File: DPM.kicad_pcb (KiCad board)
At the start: 2 copper layers, 95.9 x 90.2 mm, 27 parts, among them J1 Conn_02x12_Odd_Even, J2 Conn_02x05_Odd_Even, U1 74LS251, U25 74LS85, U28 74LS85, U3 ADG333A, U31 74LS85, U4 MCP23017_SP, U5 ADG333A, U6 ADG333A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

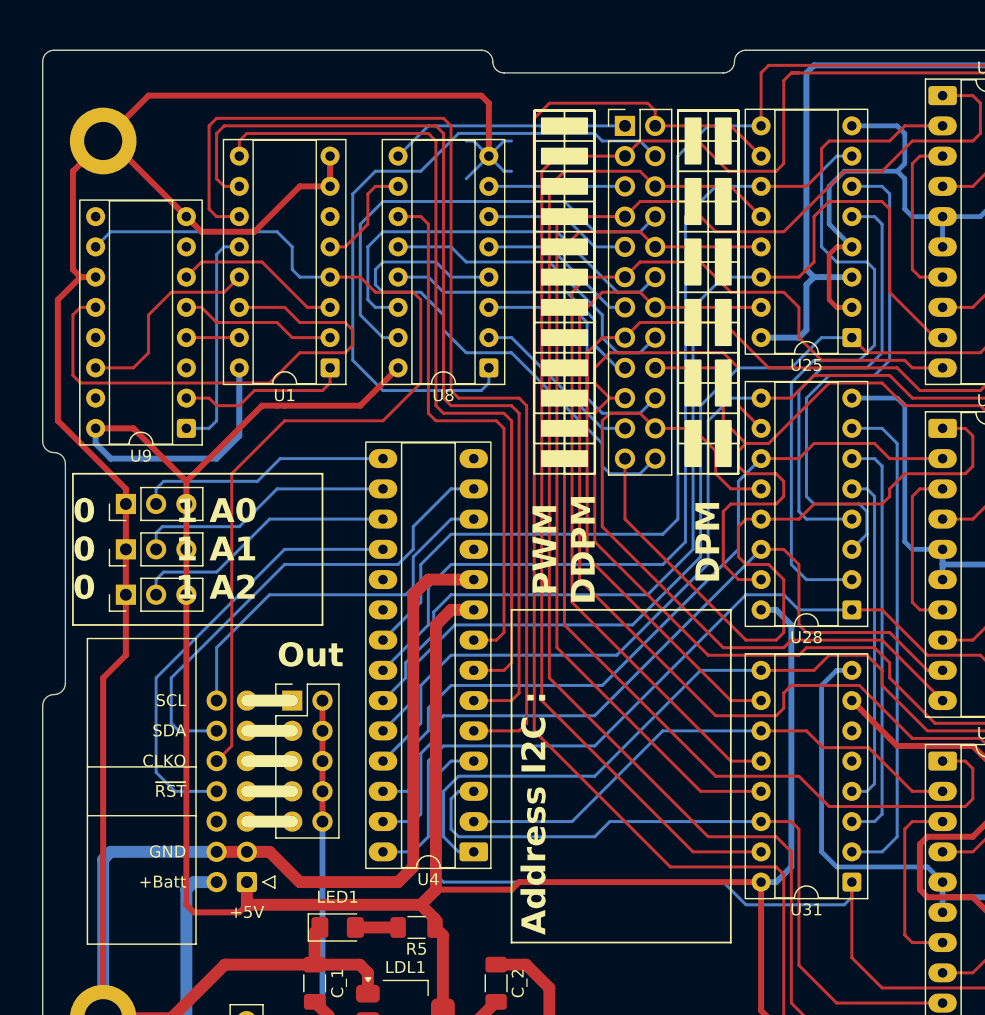
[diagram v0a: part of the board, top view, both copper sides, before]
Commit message: Nouvelle liste de prescaler : 1 2 8 16 64 256 1024 4096
git-svn-id: file:///D%5C00%20-%20Dev%20&%20Calculs%5CRepoTortoiseSVN_PCB%5CD-DPM/trunk@21 f29d8339-a183-0348-962e-9e4594cf8312
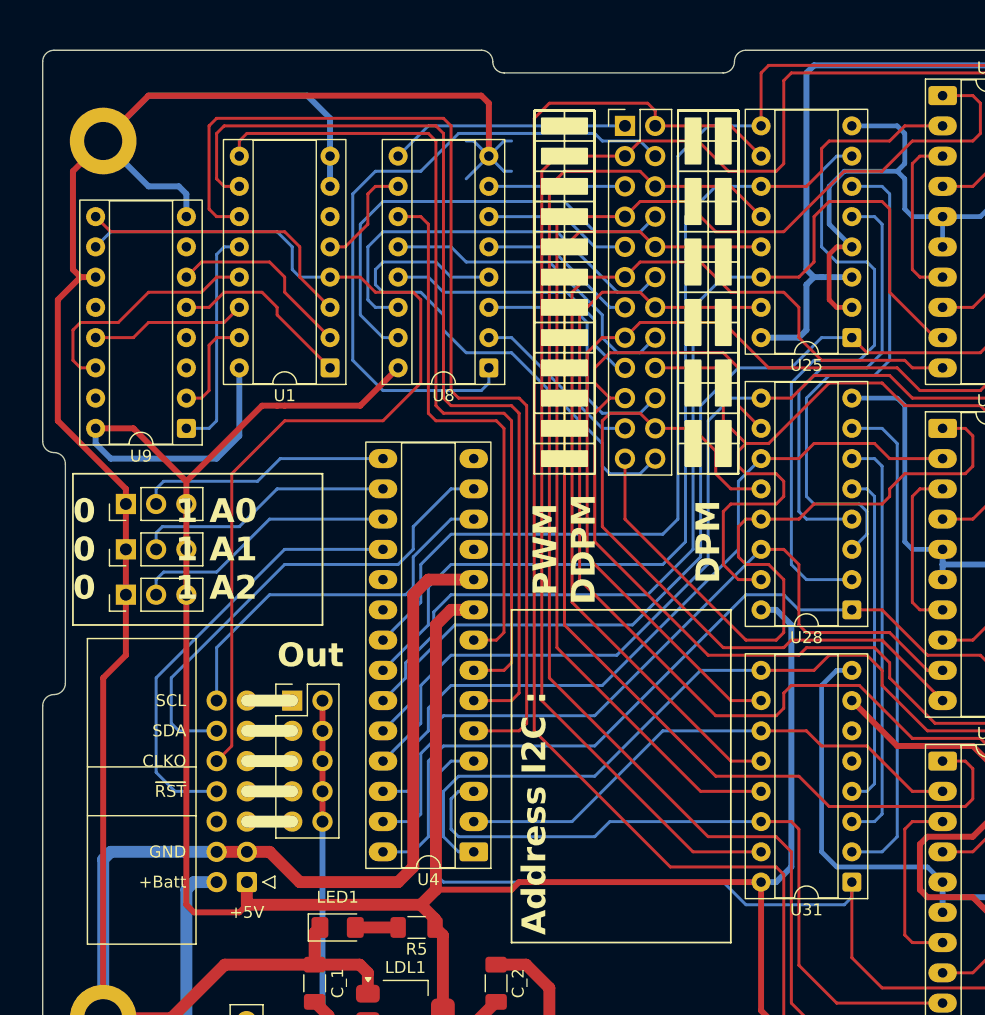
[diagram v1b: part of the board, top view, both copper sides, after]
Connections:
- U1 pad 1: /Div_64 -> /Div_16
- U1 pad 14: /Div_512 -> /Div_256
- U1 pad 15: /Div_128 -> /Div_64
- U1 pad 2: /Div_16 -> /Div_8
- U1 pad 3: /Div_8 -> /Div_2
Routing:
- net /Div_512: track 43.9 -> 0.00 mm
- net /Div_2: track 0.00 -> 24.3 mm
- net /Div_256: track 0.00 -> 13.1 mm
- net Ground: track 621.6 -> 633.7 mm
- net /Div_64: track 14.4 -> 8.78 mm
- net /Div_128: track 4.44 -> 0.00 mm
- net /Div_1024: track 17.1 -> 20.5 mm
- net /Div_16: track 13.1 -> 15.6 mm
- net /Div_8: track 14.2 -> 16.0 mm
- net /CNT_A11: track 120.4 -> 119.8 mm

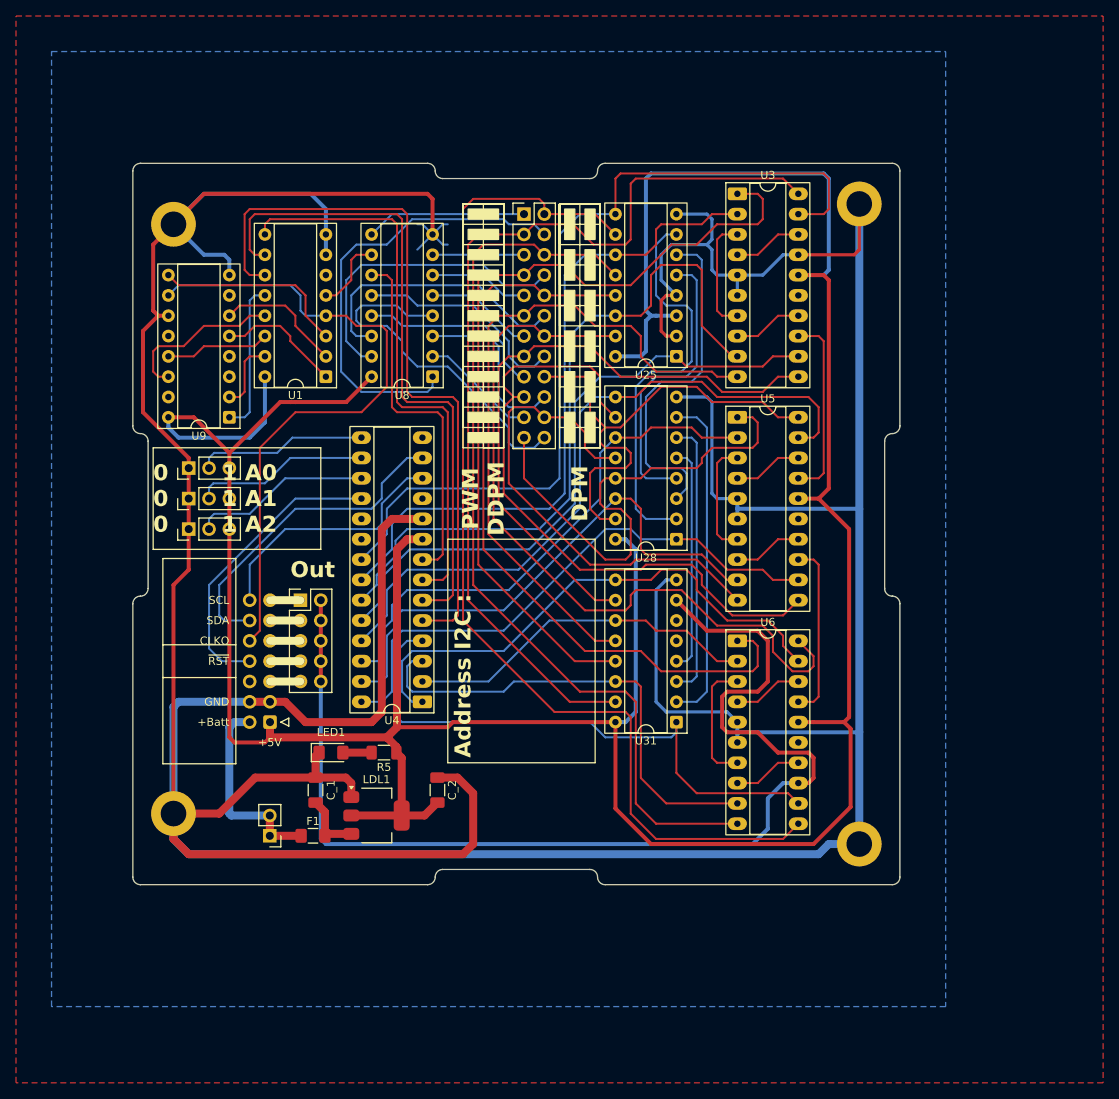
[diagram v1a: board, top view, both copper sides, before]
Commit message: - Condo UC - résintances pull-up I2C - D-latch 2G74 - routage - silkscreen
git-svn-id: file:///D%5C00%20-%20Dev%20&%20Calculs%5CRepoTortoiseSVN_PCB%5CD-DPM/trunk@22 f29d8339-a183-0348-962e-9e4594cf8312
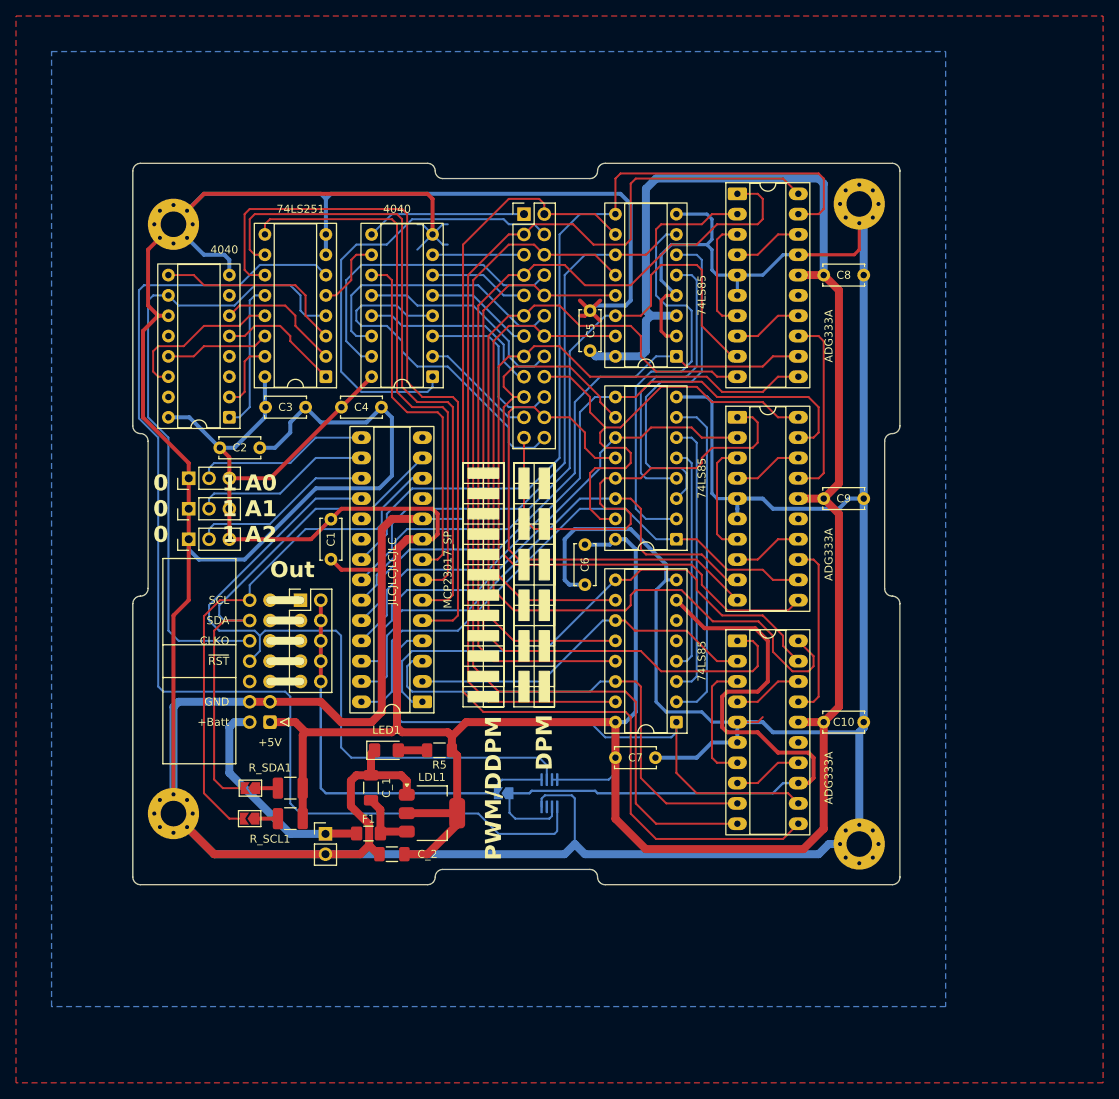
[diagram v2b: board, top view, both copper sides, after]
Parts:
- added ByPass_2G74: SolderJumper_2_Open, Jumper:SolderJumper-2_P1.3mm_Open_TrianglePad1.0x1.5mm, B.Cu at (87.6, 123.2)
- added C1: 0.1µF, Capacitor_THT:C_Disc_D5.0mm_W2.5mm_P5.00mm, F.Cu at (66.0, 93.9)
- added C10: 0.1µF, Capacitor_THT:C_Disc_D5.0mm_W2.5mm_P5.00mm, F.Cu at (132.6, 114.3)
- added C2: 0.1µF, Capacitor_THT:C_Disc_D5.0mm_W2.5mm_P5.00mm, F.Cu at (57.1, 80.0)
- added C3: 0.1µF, Capacitor_THT:C_Disc_D5.0mm_W2.5mm_P5.00mm, F.Cu at (62.9, 74.9)
- added C4: 0.1µF, Capacitor_THT:C_Disc_D5.0mm_W2.5mm_P5.00mm, F.Cu at (72.3, 74.9)
- added C5: 0.1µF, Capacitor_THT:C_Disc_D5.0mm_W2.5mm_P5.00mm, F.Cu at (98.4, 62.9)
- added C6: 0.1µF, Capacitor_THT:C_Disc_D5.0mm_W2.5mm_P5.00mm, F.Cu at (97.8, 97.1)
- added C7: 0.1µF, Capacitor_THT:C_Disc_D5.0mm_W2.5mm_P5.00mm, F.Cu at (106.6, 118.7)
- added C8: 0.1µF, Capacitor_THT:C_Disc_D5.0mm_W2.5mm_P5.00mm, F.Cu at (132.6, 58.4)
- added C9: 0.1µF, Capacitor_THT:C_Disc_D5.0mm_W2.5mm_P5.00mm, F.Cu at (132.6, 86.4)
- added Pad_SCL1: SolderJumper_2_Open, Jumper:SolderJumper-2_P1.3mm_Open_TrianglePad1.0x1.5mm, F.Cu at (55.9, 126.4)
- added Pad_SDA1: SolderJumper_2_Open, Jumper:SolderJumper-2_P1.3mm_Open_TrianglePad1.0x1.5mm, F.Cu at (56.0, 122.6)
- added R_SCL1: 4.7 kOhm, Resistor_SMD:R_1210_3225Metric_Pad1.30x2.65mm_HandSolder, F.Cu at (61.0, 126.4)
- added R_SDA1: 4.7 kOhm, Resistor_SMD:R_1210_3225Metric_Pad1.30x2.65mm_HandSolder, F.Cu at (61.0, 122.6)
- added U2: 74LVC2G74, Package_SO_AKL:SSOP-8_2.95x2.8mm_P0.65mm, B.Cu at (93.3, 123.2)
- H1, H2, H3, H4: footprint MountingHole:MountingHole_3.2mm_M3_DIN965_Pad -> MountingHole:MountingHole_3.2mm_M3_Pad_Via
- moved C_2 9.83 mm to (73.7, 130.8), turned to 0 degrees
- moved J_VIN_0 6.96 mm to (65.4, 128.3), turned to 0 degrees
- moved C_1 6.94 mm to (71.0, 122.5)
- moved F1 6.94 mm to (70.7, 128.2)
- moved LDL1 6.94 mm to (78.7, 125.7)
- moved LED1 6.94 mm to (73.0, 117.8)
- moved R5 6.94 mm to (79.6, 117.8)
- moved JP1 1.27 mm to (48.3, 91.4)
- moved JP2 1.27 mm to (48.3, 87.6)
- moved JP3 1.27 mm to (48.3, 83.8)
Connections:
- J2 pad 10: DPM -> Net-(ByPass_2G74-B)
- J2 pad 2: DPM -> Net-(ByPass_2G74-B)
- J2 pad 4: DPM -> Net-(ByPass_2G74-B)
- J2 pad 6: DPM -> Net-(ByPass_2G74-B)
- J2 pad 8: DPM -> Net-(ByPass_2G74-B)
- J_VIN_0 pad 2: VBatt -> Ground
- U1 pad 6: unconnected-(U1-~{Y}-Pad6) -> /~{Clock_loc}
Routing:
- net Ground: track 633.7 -> 792.6 mm
- net /~{Clock_loc}: track 0.00 -> 144.2 mm
- net ~{Reset}: track 37.2 -> 90.4 mm
- net Net-(ByPass_2G74-B): track 0.00 -> 52.8 mm
- net DPM: track 141.8 -> 92.9 mm
- net SCL: track 32.0 -> 65.1 mm
- net SDA: track 41.0 -> 66.2 mm
- net +5V: track 406.0 -> 425.0 mm
- net /CNT_A8: track 78.4 -> 83.7 mm
- net /CNT_A9: track 84.8 -> 90.0 mm
- net /CNT_A3: track 94.9 -> 100.1 mm
- net /CNT_A2: track 95.5 -> 100.4 mm
- net /CNT_A5: track 61.4 -> 65.7 mm
- net /CNT_A10: track 104.5 -> 108.6 mm
- net /CNT_A1: track 114.0 -> 118.1 mm
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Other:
- board text added: "JLCJLCJLCJLC"
- board text added: "PWM/DDPM"
- board text removed: "Address I2C :"
- board text removed: "PWM DDPM"

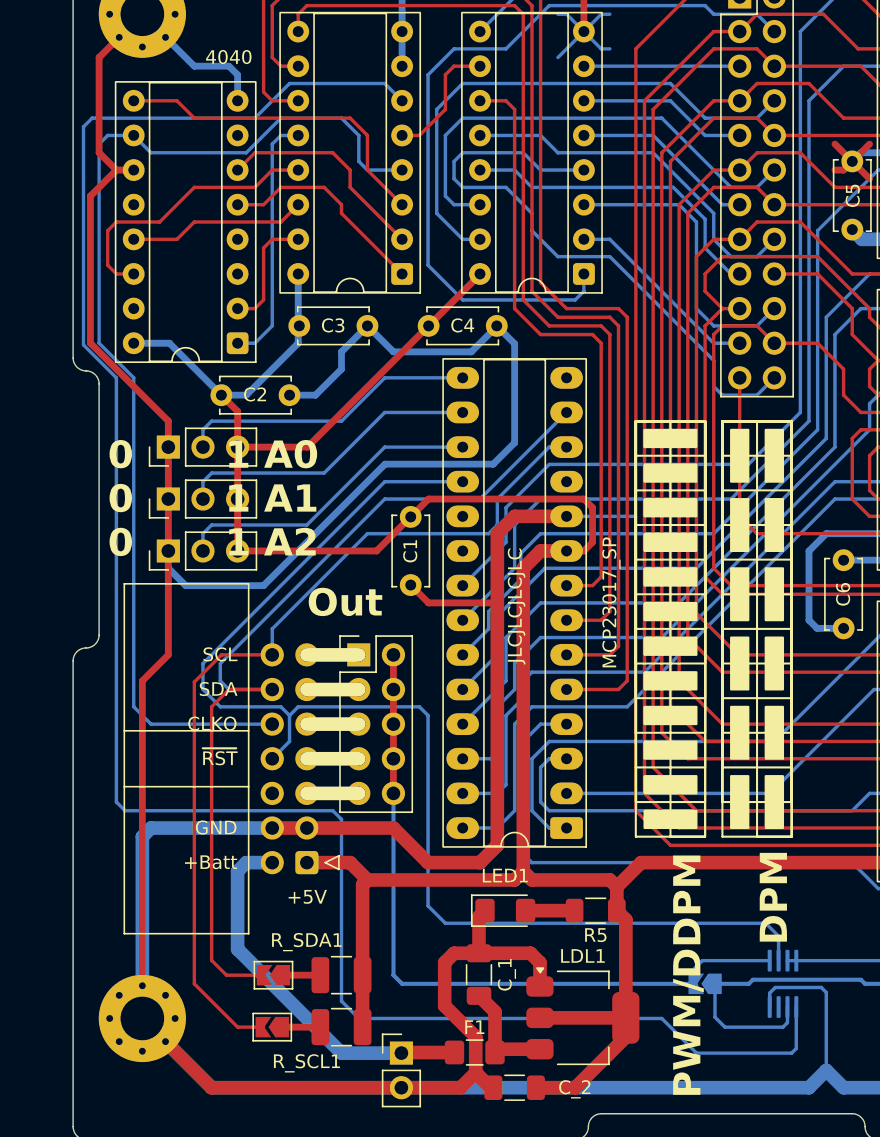
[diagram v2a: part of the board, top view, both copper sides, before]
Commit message: Correction clock du 2G74 Reroutage léger
git-svn-id: file:///D%5C00%20-%20Dev%20&%20Calculs%5CRepoTortoiseSVN_PCB%5CD-DPM/trunk@23 f29d8339-a183-0348-962e-9e4594cf8312
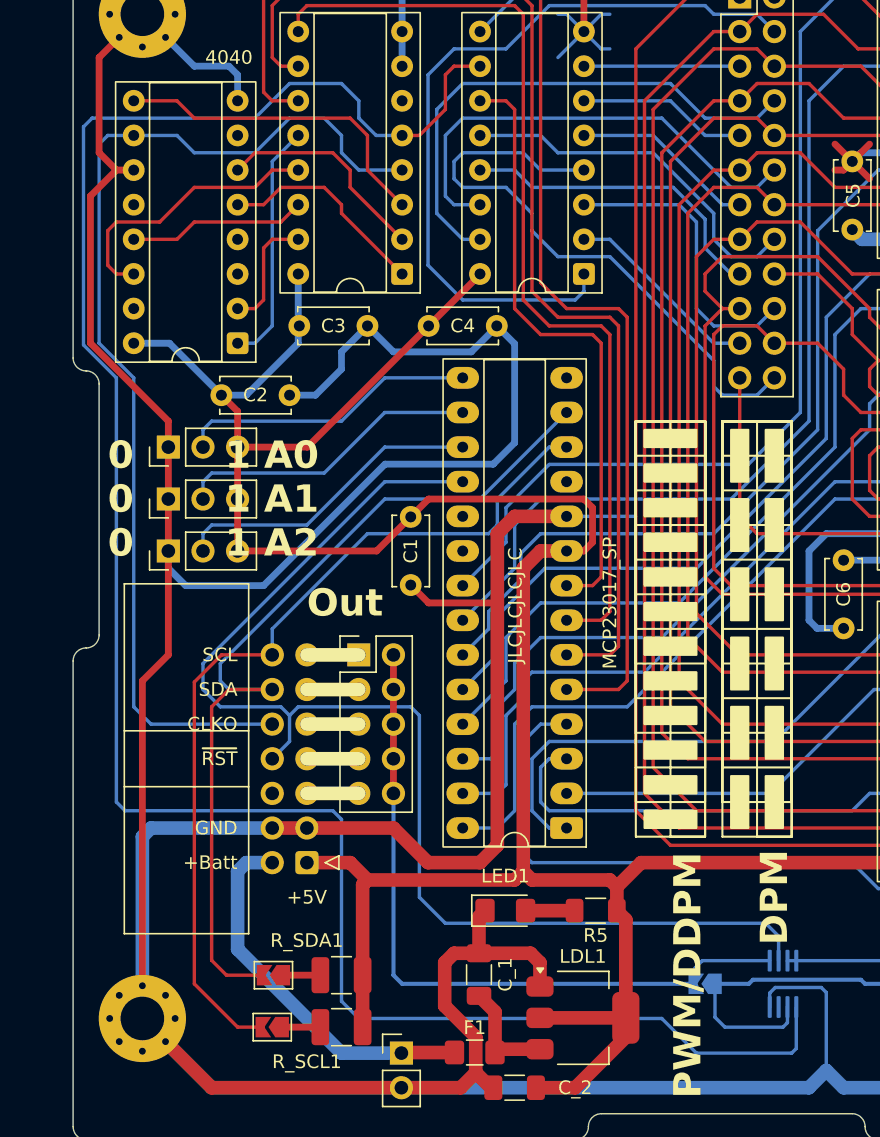
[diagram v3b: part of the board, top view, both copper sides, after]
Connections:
- U1 pad 5: Net-(U1-Y) -> /Clock_loc
- U1 pad 6: /~{Clock_loc} -> unconnected-(U1-~{Y}-Pad6)
- U2 pad 1: /~{Clock_loc} -> /Clock_loc
- U8 pad 10: Net-(U1-Y) -> /Clock_loc
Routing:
- net /Clock_loc: track 0.00 -> 155.3 mm
- net /~{Clock_loc}: track 144.2 -> 0.00 mm
- net Net-(U1-Y): track 9.31 -> 0.00 mm
- net /Div_4096: track 18.6 -> 17.8 mm
